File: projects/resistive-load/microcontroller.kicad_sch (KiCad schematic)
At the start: 32 parts, among them J5 USB4105-GF-A, J6 Conn_01x20, J7 Conn_01x03, U1 W25Q128JV, U3 RP2040, U4 MCP1702T-3302E_CB, Y1 12MHz

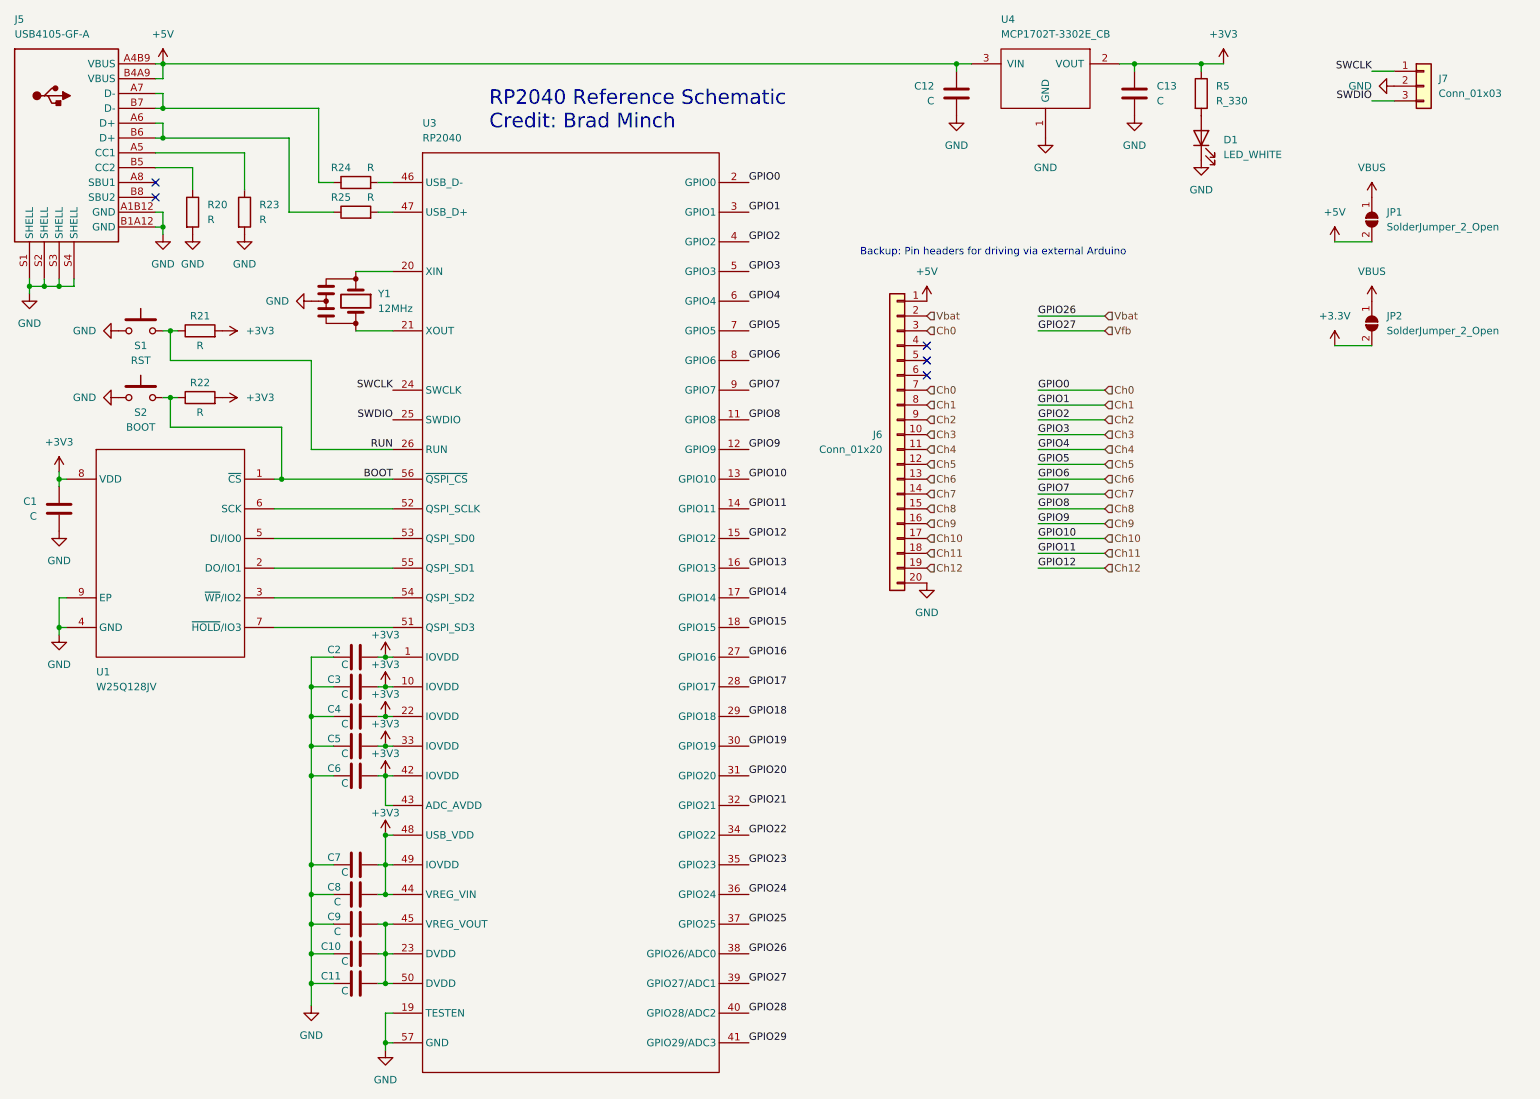
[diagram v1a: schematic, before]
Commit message: fix: update pin assignment for transistors
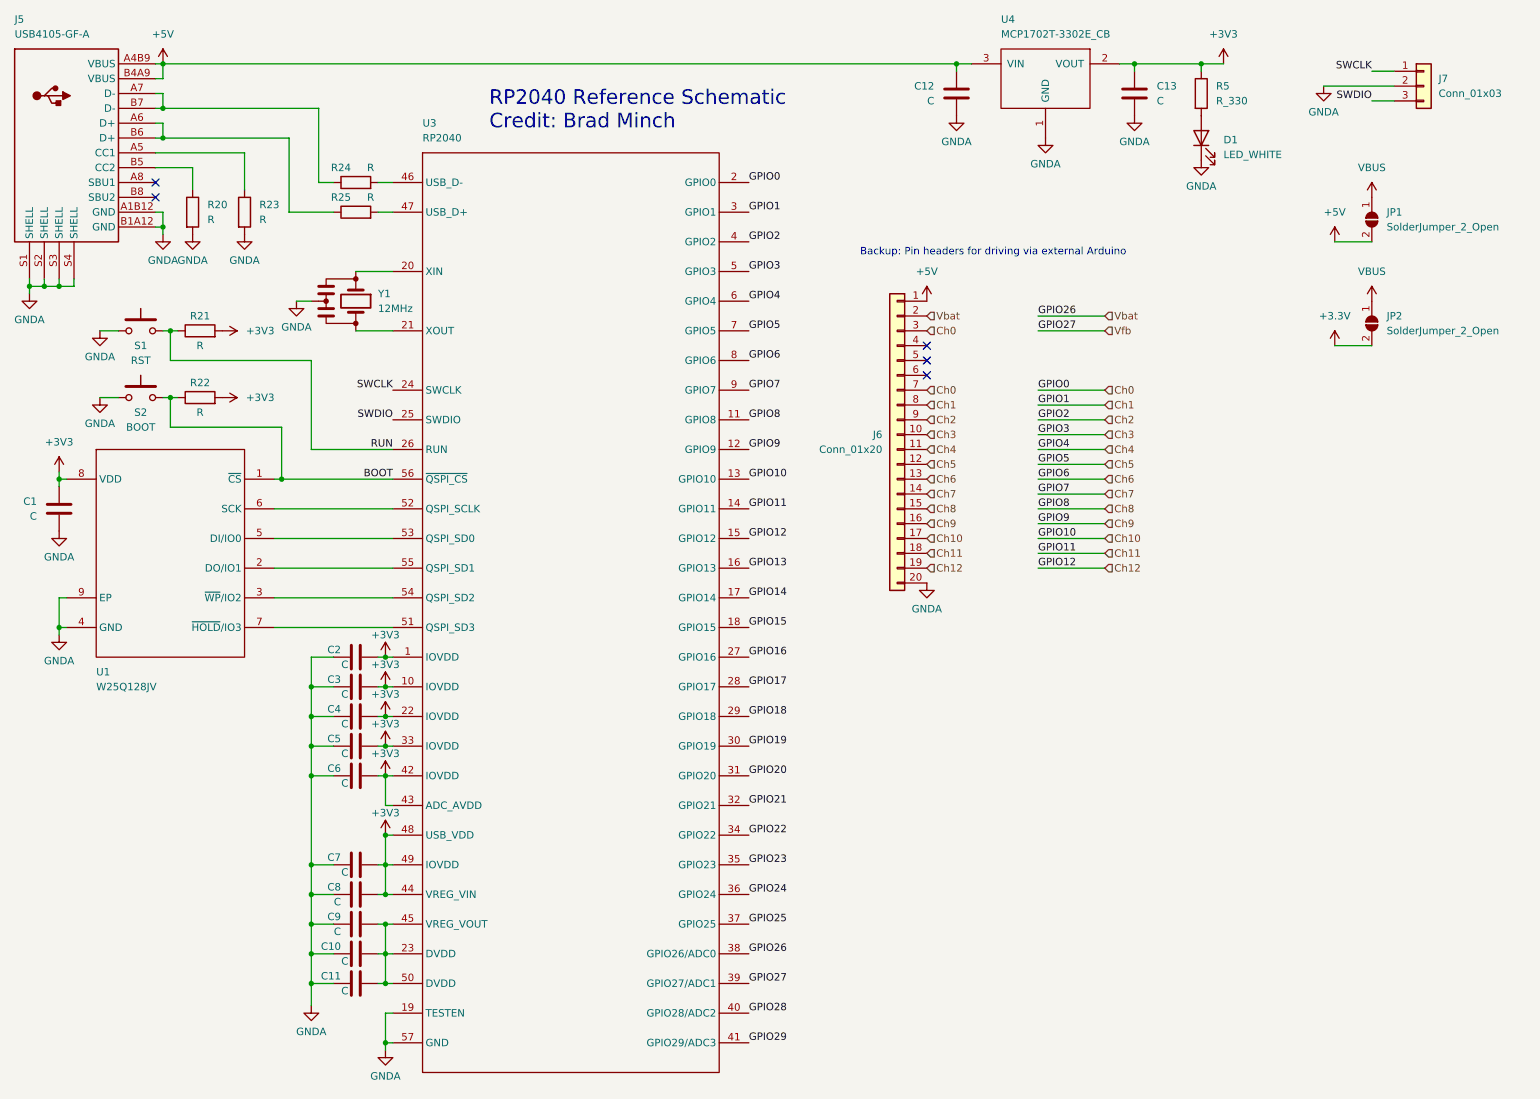
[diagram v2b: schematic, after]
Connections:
- net GND renamed GNDA
